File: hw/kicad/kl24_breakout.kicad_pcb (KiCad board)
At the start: 2 copper layers, 36.1 x 20.8 mm, 50 parts, among them J1 USB-micro-ab, P1 TST, P10 TST, P11 TST, P12 TST, P13 TST, P14 TST, P15 TST, P16 TST, P17 TST, P18 TST, P19 TST, P2 TST, P20 TST, P21 TST, P22 TST, P23 TST, P24 TST, P25 TST, P26 TST, P27 TST, P28 TST, P29 TST, P3 TST, P30 TST, P31 TST, P32 TST, P33 +5V, P34 GND, P35 SWD_VCC, P36 SWDIO, P37 SWCLK, P38 NRESET, P39 SWD_GND, P4 TST, P5 TST, P6 TST, P7 TST, P8 TST, P9 TST, U1 MKL24Z64VFM4, X1 CRYSTAL

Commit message: add some decoupling caps to +5 and +3.3 and nreset update to v0.2 replot
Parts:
- added C3: 0.1uF, SM0603, B.Cu at (117.0, 76.2)
- added C4: 0.1uF, SM0603, B.Cu at (137.7, 77.1)
- added C5: 0.1uF, SM0603, B.Cu at (139.7, 64.8)
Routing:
- net 19: track 18.4 -> 22.7 mm
- net 15: track 46.9 -> 48.5 mm
- net 6: track 31.2 -> 32.3 mm
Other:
- board text added: "MKL24Z64VFM4 Breakout v0.2 git.io/7Xh66w oct-2013"
- board text removed: "MKL24Z64VFM4 Breakout v0.1 git.io/7Xh66w oct-2013"

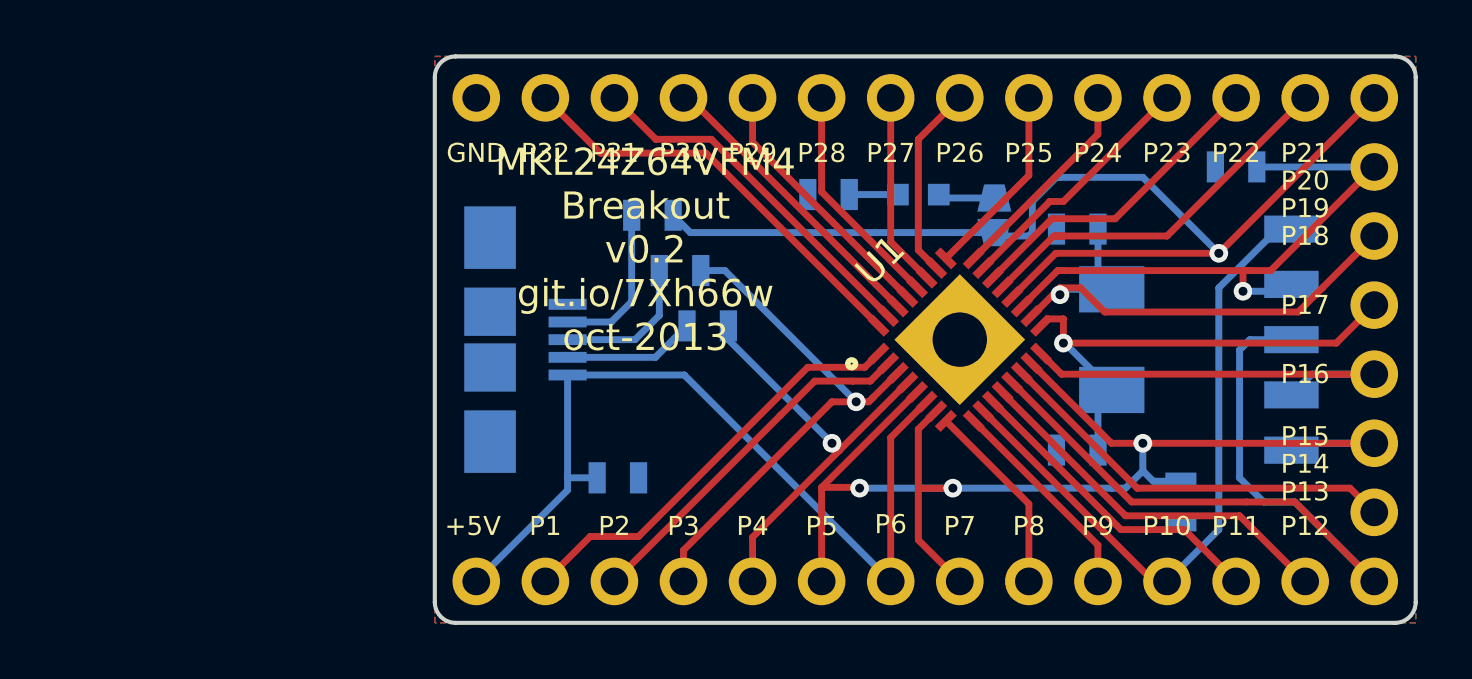
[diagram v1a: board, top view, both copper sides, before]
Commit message: - add 10k pullup on nreset
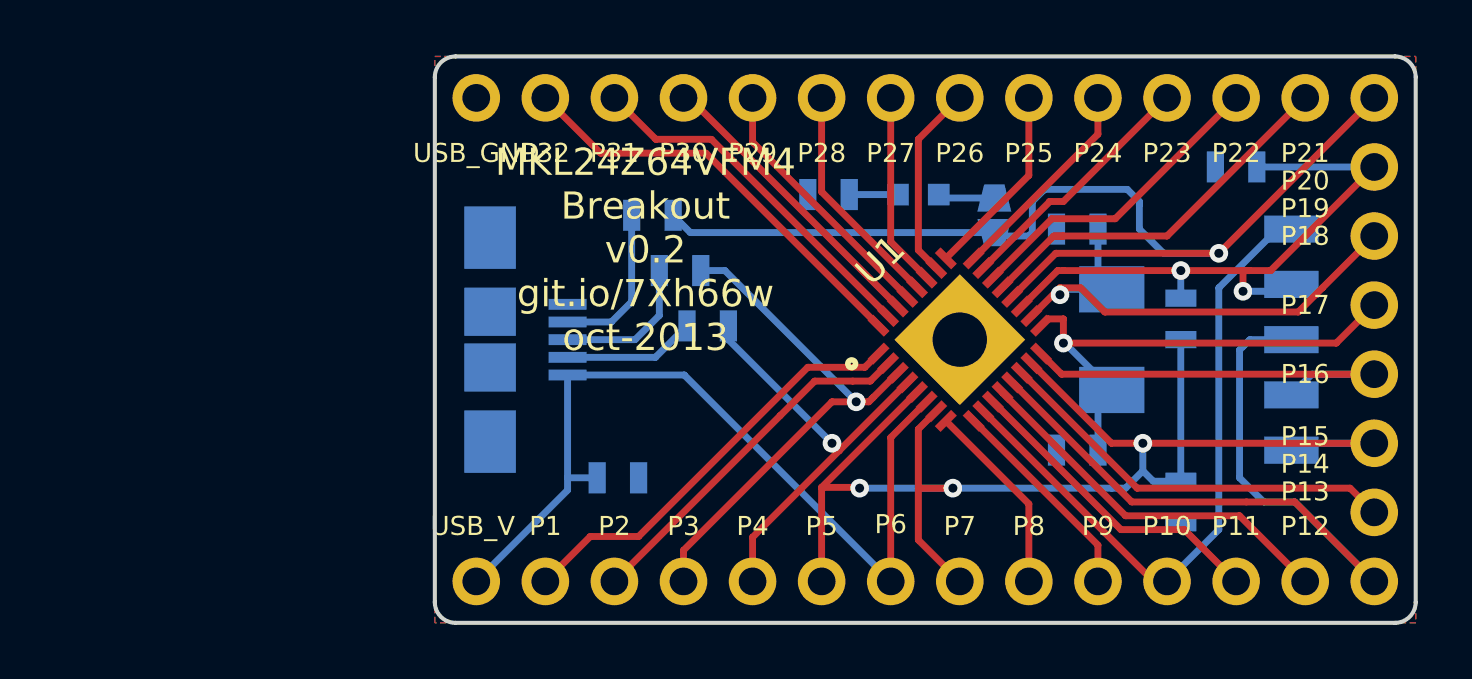
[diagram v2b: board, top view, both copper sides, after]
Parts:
- added R5: 10K, SM0603, B.Cu at (137.7, 70.4)
- P33: value +5V -> USB_V
- P34: value GND -> USB_GND
- P35: value SWD_VCC -> VCC
- P38: value NRESET -> NRST
- P39: value SWD_GND -> GND
- turned C5 to 0 degrees
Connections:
- C5 pad 1: 19 -> 16
- C5 pad 2: 16 -> 19
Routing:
- net 15: track 48.5 -> 53.7 mm
- net 19: track 22.7 -> 23.8 mm, vias 1 -> 2

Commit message: - add gerbers - update pcb
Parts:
- P33: value USB_V -> +5v
- P34: value USB_GND -> GND
- P35: value VCC -> SWD_VCC
- P38: value NRST -> NRESET
- P39: value GND -> SWD_GND

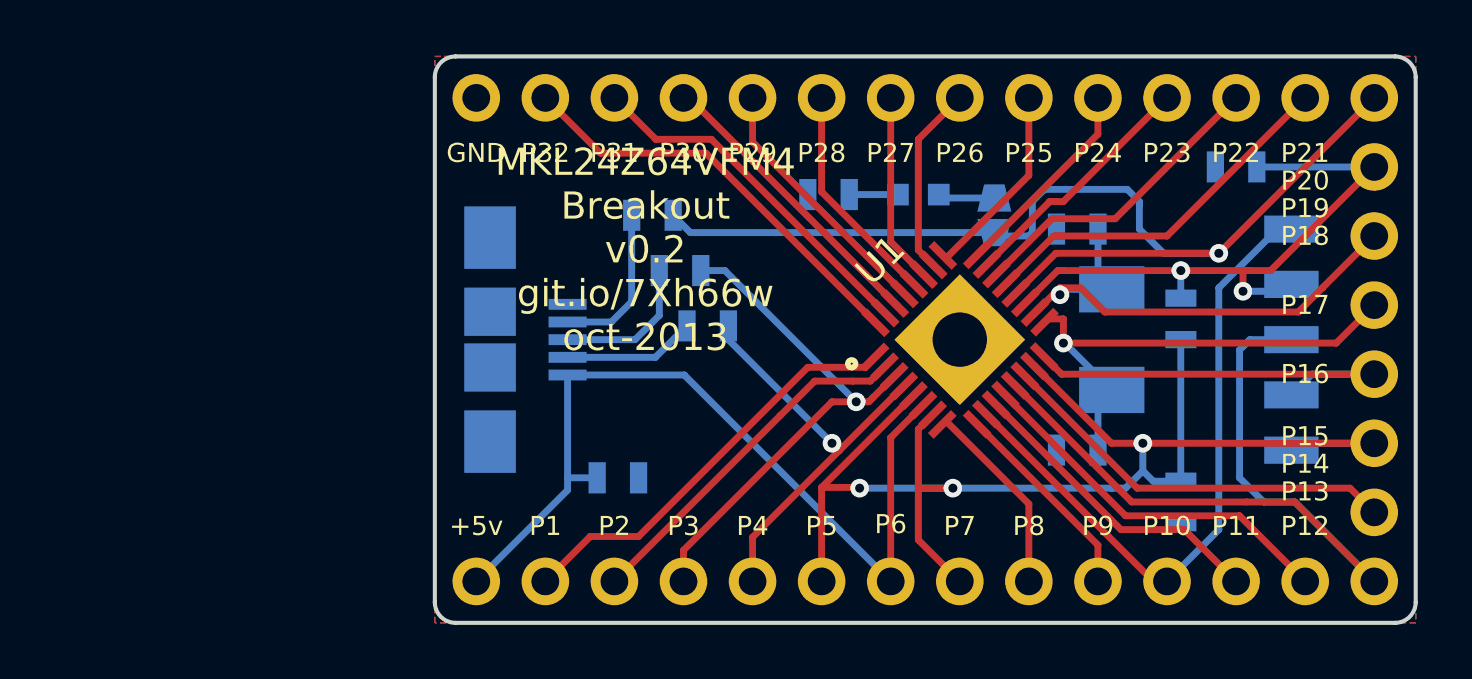
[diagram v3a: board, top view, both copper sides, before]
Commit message: - remove power pin breakout. add arm 10 pin header.
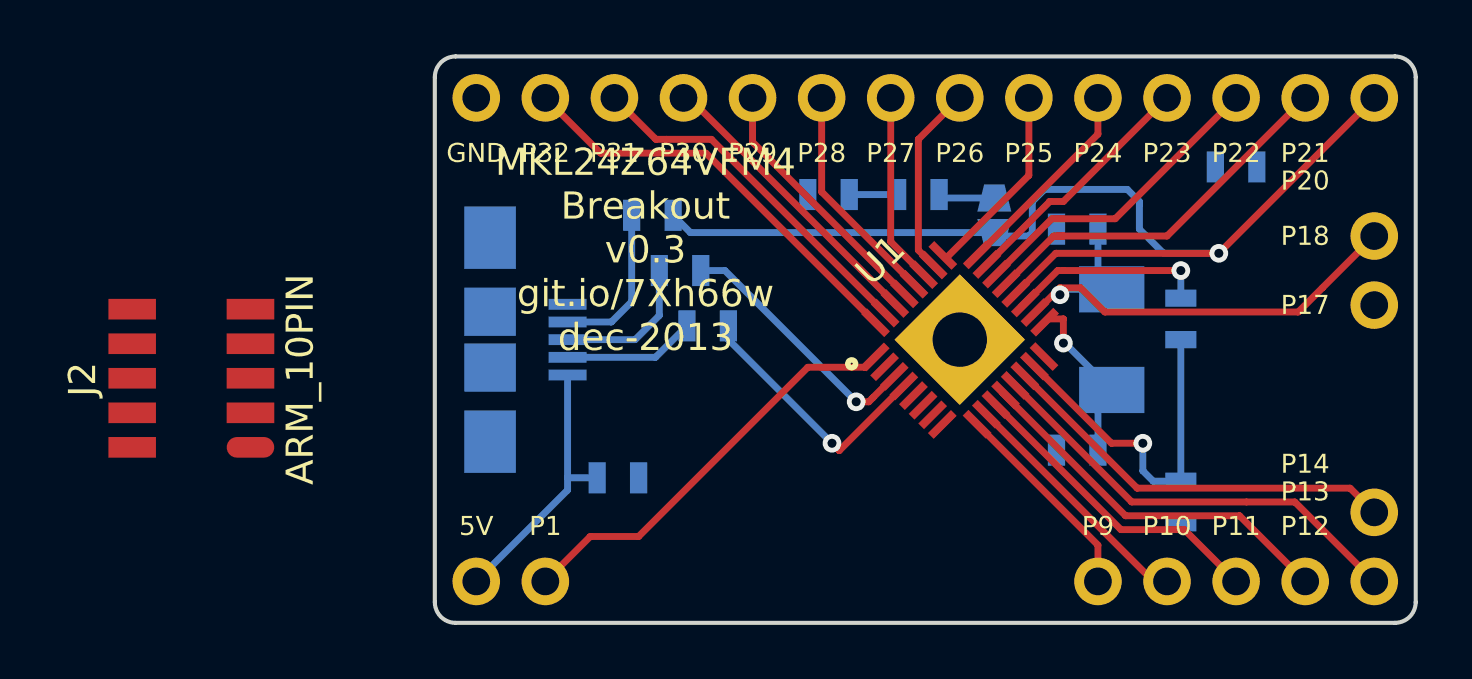
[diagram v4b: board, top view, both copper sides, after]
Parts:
- removed P15, P16, P19, P2, P3, P4, P5, P6, P7, P8: TST, TEST_0.100
- removed P35: SWD_VCC, smd_simple_pad
- removed P36: SWDIO, smd_simple_pad
- removed P37: SWCLK, smd_simple_pad
- removed P38: NRESET, smd_simple_pad
- removed P39: SWD_GND, smd_simple_pad
- added J2: ARM_10PIN, ARM_10_PIN_SMT, F.Cu at (101.3, 72.6)
- D1: footprint LED-0603 -> SM0603
- P33: value +5v -> 5V
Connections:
- net 15 renamed 3.3V_SUPPLY
- net 16 renamed GND
- net 19 renamed nreset
- net 3 renamed N-0000031
- net 4 renamed N-0000032
- net 6 renamed USB_VBUS
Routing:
- net 3.3V_SUPPLY: track 53.7 -> 13.1 mm, vias 3 -> 1
- net GND: track 36.5 -> 0.00 mm
- net USB_VBUS: track 32.3 -> 10.1 mm
- net nreset: track 23.8 -> 7.41 mm, vias 2 -> 1
- net 10: track 24.5 -> 9.35 mm
- net 13: track 29.6 -> 16.3 mm
- net 17: track 19.5 -> 7.45 mm
- net N-0000031: track 19.6 -> 9.69 mm
- net N-0000032: track 15.9 -> 9.82 mm
- removed copper zone on B.Cu, net GND
- removed copper zone on F.Cu, net GND
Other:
- board text added: "MKL24Z64VFM4 Breakout v0.3 git.io/7Xh66w dec-2013"
- board text removed: "MKL24Z64VFM4 Breakout v0.2 git.io/7Xh66w oct-2013"

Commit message: - remove crystal
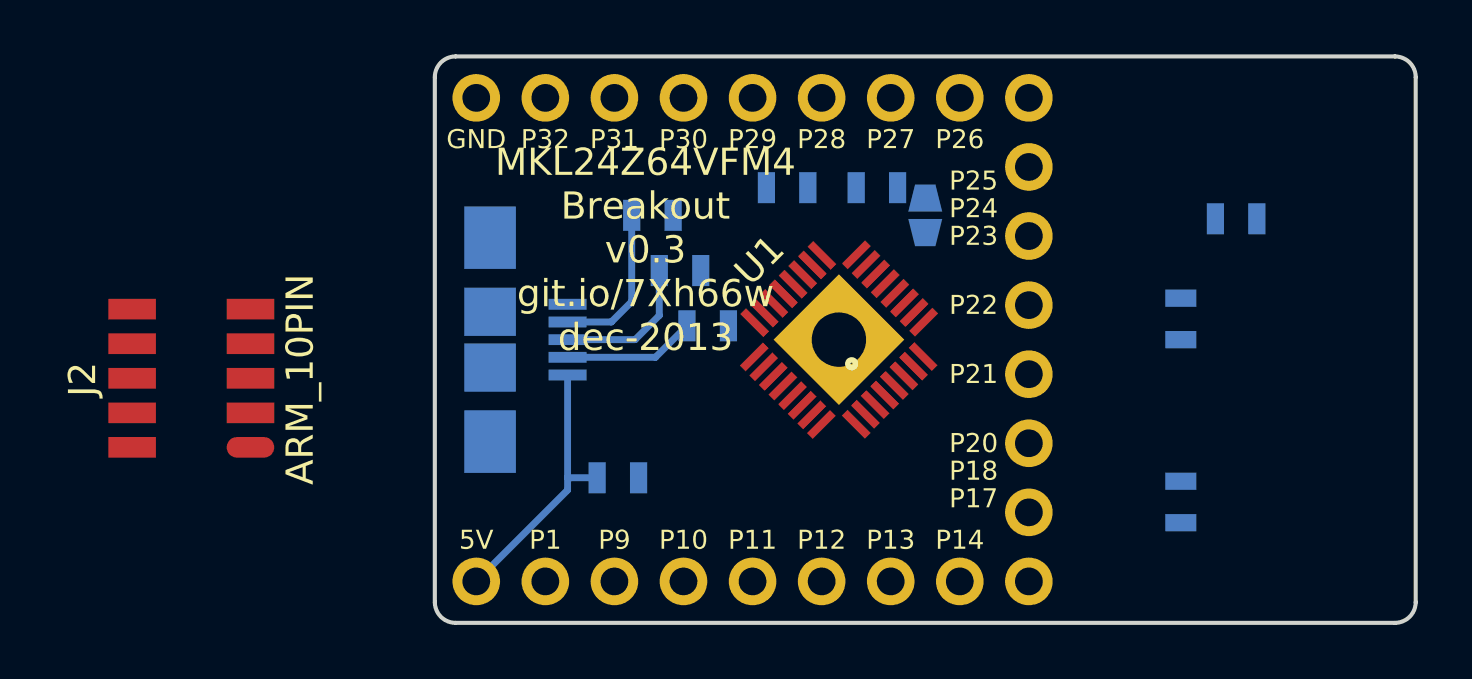
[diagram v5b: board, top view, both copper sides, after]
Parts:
- removed C1, C2: 22pF, SM0603
- removed X1: CRYSTAL, XTAL_7A-8-000MAAE-T
- moved P20 18.0 mm to (132.1, 74.9)
- moved P12 17.8 mm to (124.5, 80.0)
- moved P10 17.8 mm to (119.4, 80.0)
- moved P13 17.8 mm to (127.0, 80.0)
- moved P9 17.8 mm to (116.8, 80.0)
- moved P11 17.8 mm to (121.9, 80.0)
- moved P17 16.3 mm to (132.1, 80.0)
- moved P18 16.3 mm to (132.1, 77.5)
- moved P14 15.5 mm to (129.5, 80.0)
- moved P21 14.4 mm to (132.1, 72.4)
- moved P22 10.8 mm to (132.1, 69.8)
- moved P23 7.18 mm to (132.1, 67.3)
- moved U1 4.44 mm to (125.1, 71.1)
- moved P24 3.59 mm to (132.1, 64.8)
- moved JP1 2.54 mm to (128.3, 66.5)
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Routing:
- net 20: track 39.7 -> 0.00 mm, vias 1 -> 0
- net 18: track 19.2 -> 0.00 mm, vias 1 -> 0
- net 13: track 16.3 -> 0.00 mm
- net 1: track 15.7 -> 0.00 mm
- net 32: track 15.7 -> 0.00 mm
- net 14: track 15.1 -> 0.00 mm
- net 21: track 14.3 -> 0.00 mm
- net 12: track 14.0 -> 0.00 mm
- net 31: track 13.4 -> 0.00 mm
- net 3.3V_SUPPLY: track 13.1 -> 0.00 mm, vias 1 -> 0
- net 11: track 11.7 -> 0.00 mm
- net 22: track 11.7 -> 0.00 mm
- net 30: track 11.1 -> 0.00 mm
- net N-0000010: track 9.82 -> 0.00 mm, vias 1 -> 0
- net N-000004: track 9.69 -> 0.00 mm, vias 1 -> 0
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
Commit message: - edge
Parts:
- moved J2 25.8 mm to (127.0, 71.1)
- moved U1 6.35 mm to (118.7, 71.1)
- moved D1 1.49 mm to (125.1, 66.0)
- moved R4 1.37 mm to (121.9, 66.0)
- moved JP1 0.81 mm to (127.6, 66.0)
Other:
- board size 36.1 x 20.8 mm -> 23.4 x 20.8 mm
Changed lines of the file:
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@@
     (links 60)
     (no_connects 55)
-    (area 96.5805 53.170001 157.858333 82.812)
+    (area 96.5805 59.496 157.858333 82.812)
     (thickness 1.6)
     (drawings 11)
@@
   )
   (module jmp_small (layer B.Cu)
-    (at 128.27 66.548)
+    (at 127.635 66.04)
     (fp_text reference JP1 (at 2.032 -0.762) (layer B.SilkS)
       (effects (font (size 0.7 0.7) (thickness 0.15)) (justify mirror))
@@
   )
   (module SM0603 (layer B.Cu)
-    (at 123.19 65.532 180)
+    (at 121.92 66.04 180)
     (attr smd)
     (fp_text reference R4 (at -1.016 1.27 180) (layer B.SilkS)
@@
   )
   (module MKL24Z64VFM4 (layer F.Cu)
-    (at 125.095 71.12 45)
+    (at 118.745 71.12 45)
     (fp_text reference U1 (at 0 -4.130918 45) (layer F.SilkS)
       (effects (font (size 1 1) (thickness 0.15)))
@@
   )
   (module SM0603 (layer B.Cu)
-    (at 126.492 65.532 180)
+    (at 125.095 66.04 180)
     (attr smd)
     (fp_text reference D1 (at 0 0 180) (layer B.SilkS)
@@
   )
   (module ARM_10_PIN_SMT (layer F.Cu)
-    (at 101.2825 72.5805 90)
-    (fp_text reference J2 (at 0 -4 90) (layer F.SilkS)
-      (effects (font (size 1 1) (thickness 0.15)))
-    )
-    (fp_text value ARM_10PIN (at 0 4 90) (layer F.SilkS)
+    (at 127 71.12 90)
+    (fp_text reference J2 (at -4.064 1.016 180) (layer F.SilkS)
+      (effects (font (size 1 1) (thickness 0.15)))
+    )
+    (fp_text value ARM_10PIN (at 0 4 90) (layer F.SilkS) hide
       (effects (font (size 1 1) (thickness 0.15)))
     )
@@
     )
   )
+  (gr_line (start 110.236 62.23) (end 110.236 80.01) (angle 90) (layer Edge.Cuts) (width 0.15))
+  (gr_arc (start 111.76 62.23) (end 110.236 62.23) (angle 90) (layer Edge.Cuts) (width 0.15))
+  (gr_line (start 133.604 80.01) (end 133.604 62.23) (angle 90) (layer Edge.Cuts) (width 0.15))
+  (gr_line (start 111.76 81.534) (end 132.08 81.534) (angle 90) (layer Edge.Cuts) (width 0.15))
+  (gr_line (start 132.08 60.706) (end 111.506 60.706) (angle 90) (layer Edge.Cuts) (width 0.15))
+  (gr_arc (start 132.08 80.01) (end 133.604 80.01) (angle 90) (layer Edge.Cuts) (width 0.15))
+  (gr_arc (start 111.76 80.01) (end 111.76 81.534) (angle 90) (layer Edge.Cuts) (width 0.15))
+  (gr_arc (start 132.08 62.23) (end 132.08 60.706) (angle 90) (layer Edge.Cuts) (width 0.15))
   (gr_text "MKL24Z64VFM4\nBreakout\nv0.3\ngit.io/7Xh66w\ndec-2013" (at 117.983 67.818) (layer F.SilkS)
     (effects (font (size 1 1) (thickness 0.25)))
@@
   )
   (gr_circle (center 125.5649 72.009) (end 125.7046 72.0471) (layer F.SilkS) (width 0.2))
-  (gr_line (start 110.236 80.772) (end 110.236 61.468) (angle 90) (layer Edge.Cuts) (width 0.15))
-  (gr_arc (start 110.998 80.772) (end 110.998 81.534) (angle 90) (layer Edge.Cuts) (width 0.15))
-  (gr_line (start 145.542 81.534) (end 110.998 81.534) (angle 90) (layer Edge.Cuts) (width 0.15))
-  (gr_arc (start 110.998 61.468) (end 110.236 61.468) (angle 90) (layer Edge.Cuts) (width 0.15))
-  (gr_line (start 145.542 60.706) (end 110.998 60.706) (angle 90) (layer Edge.Cuts) (width 0.15))
-  (gr_line (start 146.304 80.772) (end 146.304 61.468) (angle 90) (layer Edge.Cuts) (width 0.15))
-  (gr_arc (start 145.542 80.772) (end 146.304 80.772) (angle 90) (layer Edge.Cuts) (width 0.15))
-  (gr_arc (start 145.542 61.468) (end 145.542 60.706) (angle 90) (layer Edge.Cuts) (width 0.15))
   (segment (start 117.475 66.548) (end 117.475 69.723) (width 0.254) (layer B.Cu) (net 29))
   (segment (start 116.728 70.47) (end 117.475 69.723) (width 0.254) (layer B.Cu) (net 29))
